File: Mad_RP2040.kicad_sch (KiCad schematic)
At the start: 77 parts, among them J1 USB_C_Receptacle, SW1 RotaryEncoder_Switch, SW11 SW_SPST, SW12 SW_SPST, SW13 SW_SPST, SW14 SW_SPST, SW16 SW_SPST, SW17 SW_SPST, SW18 SW_SPST, SW19 SW_SPST, SW2 SW_SPST, SW3 SW_SPST, SW4 SW_SPST, SW6 SW_SPST, SW7 SW_SPST, SW8 SW_SPST, SW9 SW_SPST, T1 Tab, T2 Tab, T3 Tab, T4 Tab, U1 PCB, U2 ECMF02-2AMX6

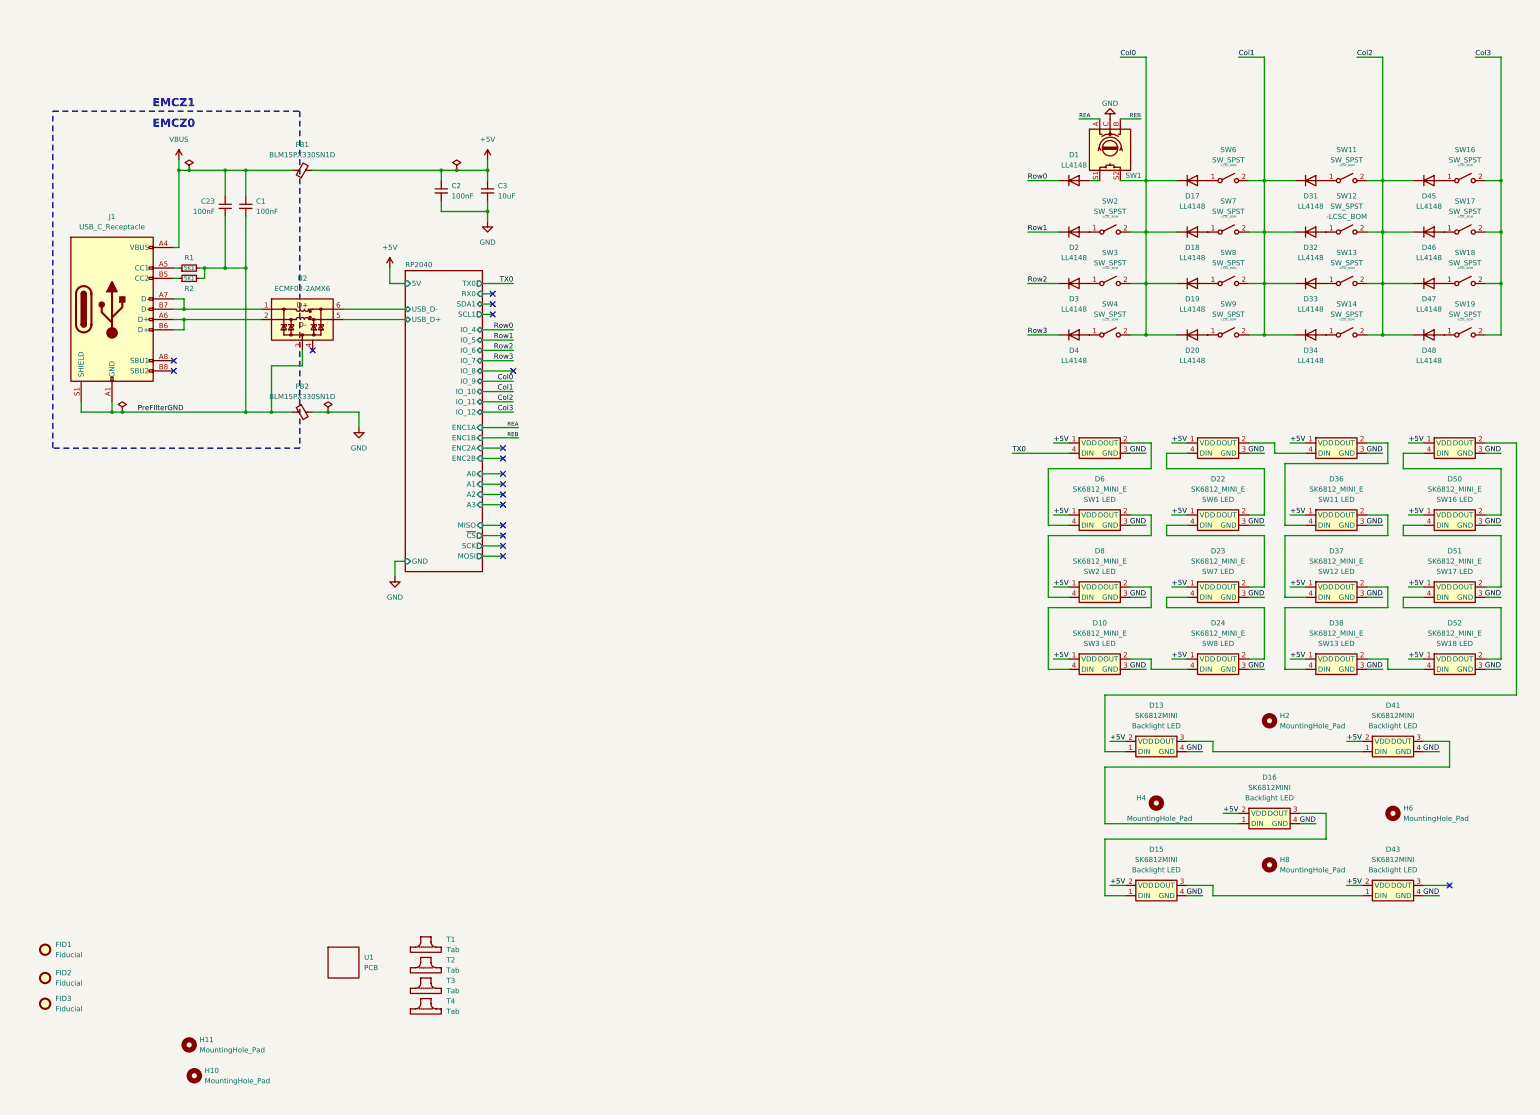
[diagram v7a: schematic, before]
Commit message: Review Schematic, Add TRS connector. Continue routing
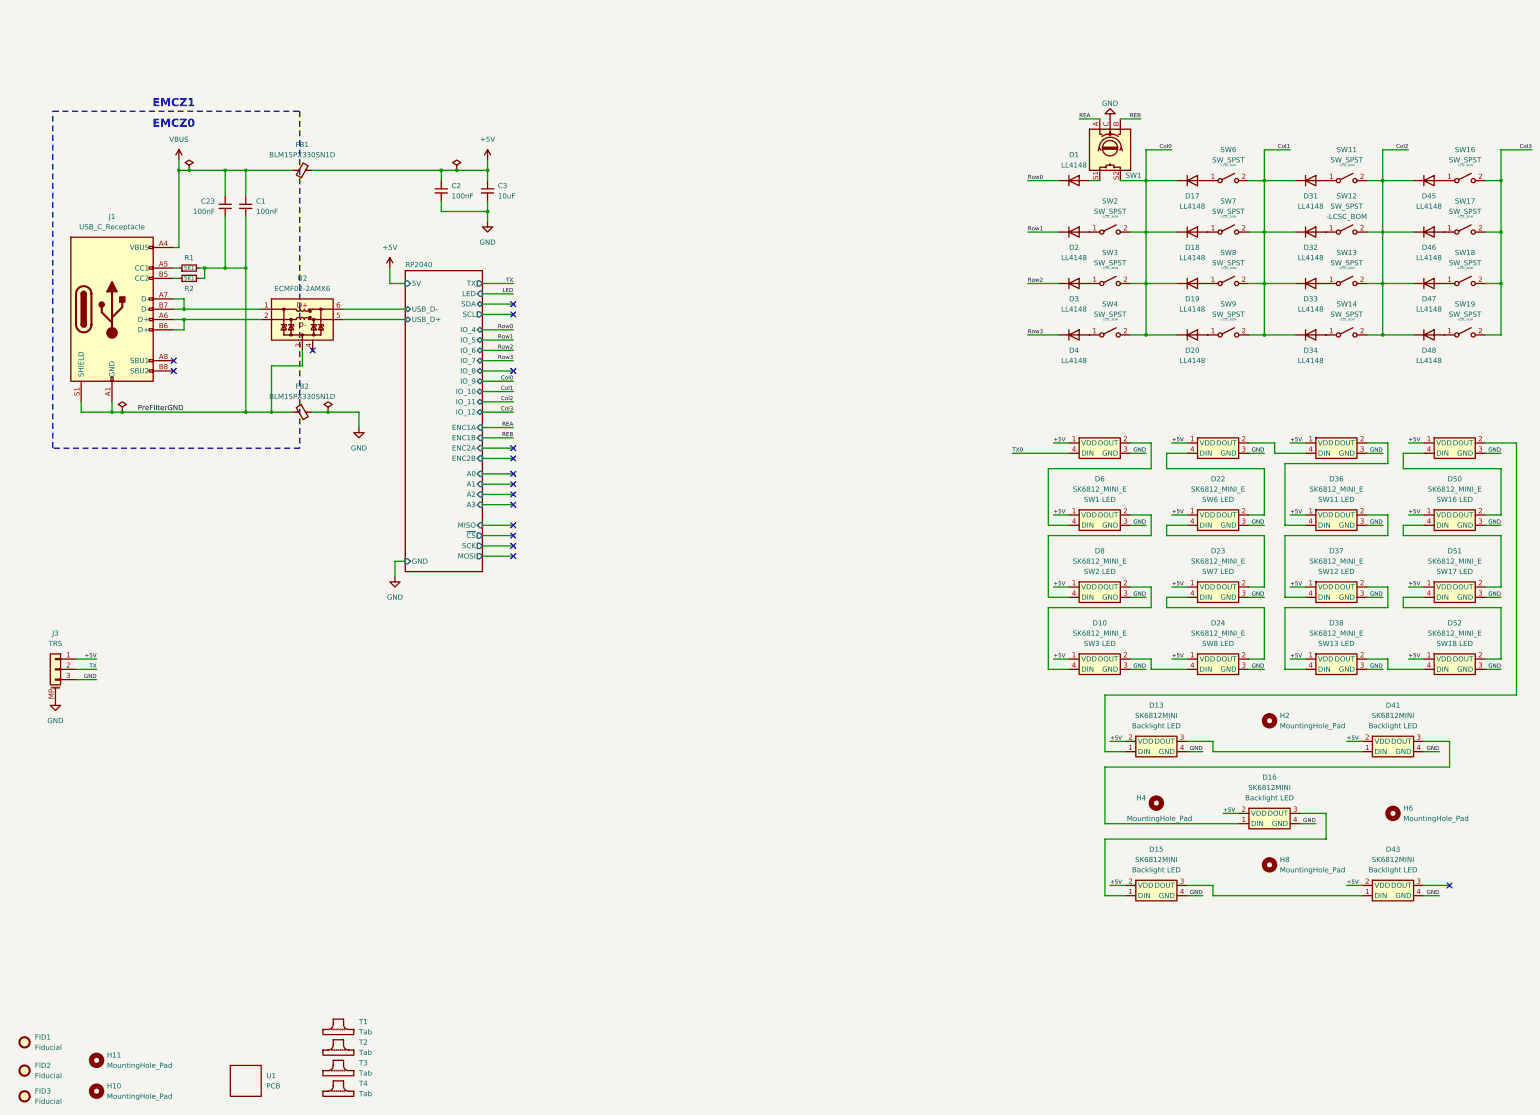
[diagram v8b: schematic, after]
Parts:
- added J3: TRS, Mad_Footprints:SM03B-GHS, symbol Connector_Generic_MountingPin:Conn_01x03_MountingPin
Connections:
- net +5V: now also J3.1 (Pin_1)
- net GND: now also J3.3 (Pin_3), J3.MP (MountPin)
- new net TX: J3.2 (Pin_2)
- no-connect marks 18 -> 17
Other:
- sheet RP2040 ports: added LED, SCL, SDA, TX; removed RX0, SCL1, SDA1, TX0
- moved on the sheet: FID1, FID2, FID3, H10, H11, T1, T2, T3, T4, U1
